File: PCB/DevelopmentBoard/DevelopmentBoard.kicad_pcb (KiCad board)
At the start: 2 copper layers, 128.3 x 64.8 mm, 37 parts, among them IC1 FE1.1S_USB_Controller, J1 Conn_01x04_MountingPin, J2 USB-A, J3 USB-A, J4 CRJ007_RJ45, U1 Pi_CM4, U2 Barometer_Grove, U3 D24V22F5, U4 Micro-USB, U5 VN-100_Breakout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

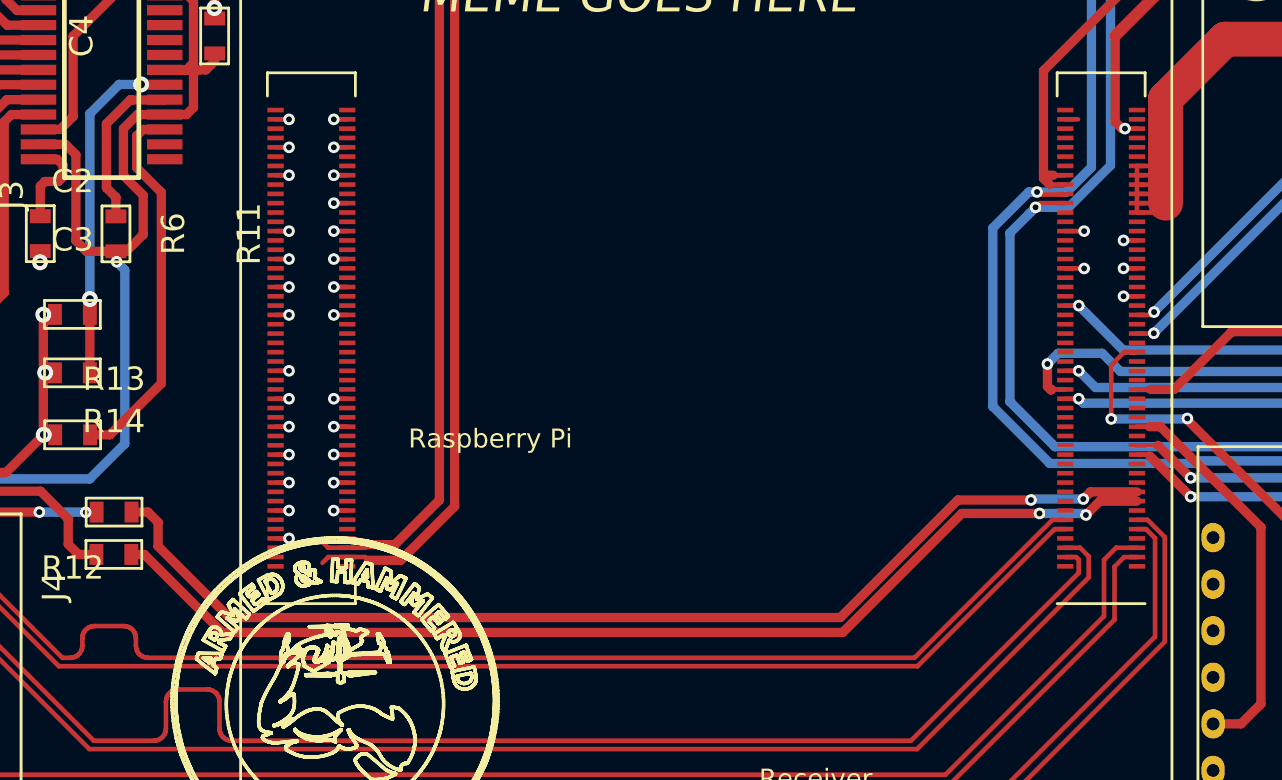
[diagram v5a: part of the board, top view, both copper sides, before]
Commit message: Adjusted USB D0 trace thickness
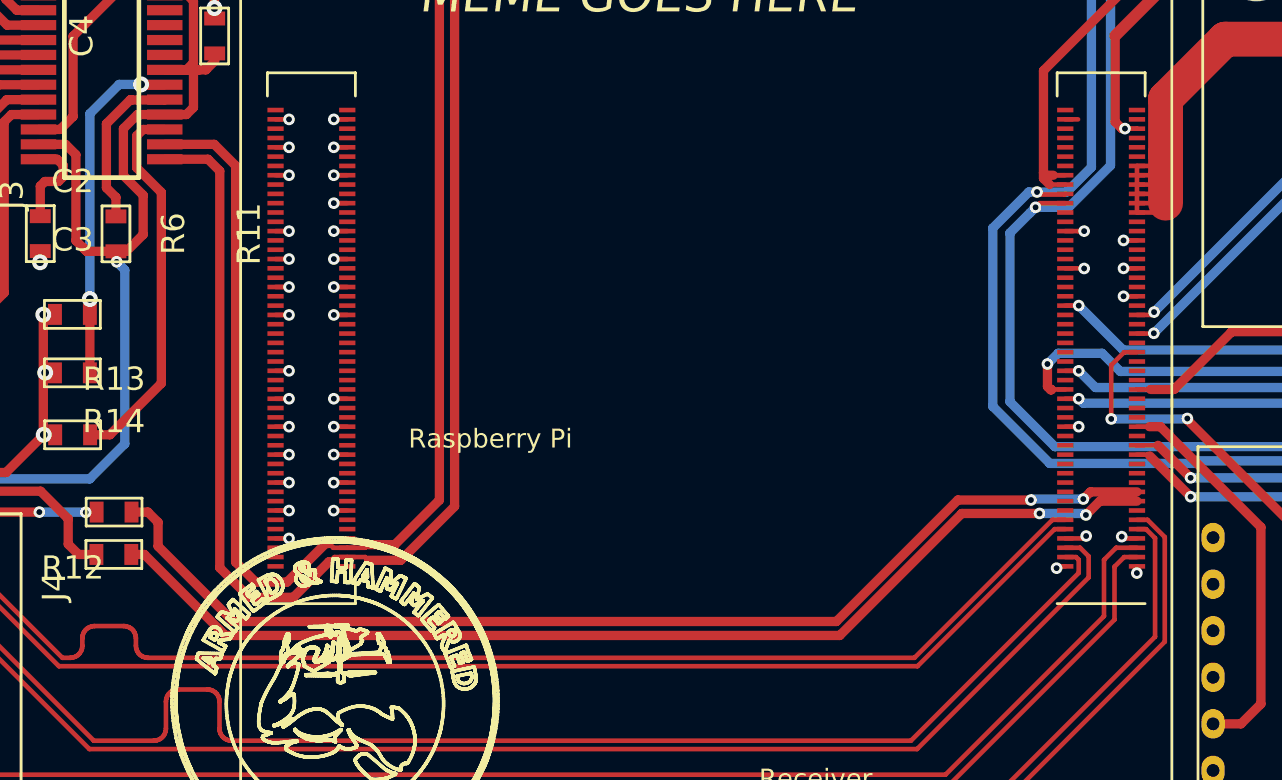
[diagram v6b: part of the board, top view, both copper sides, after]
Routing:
- net /D0+: track 42.8 -> 67.5 mm
- net /D0-: track 45.2 -> 69.9 mm
- net GND: track 27.6 -> 30.5 mm, vias 41 -> 46
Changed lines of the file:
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@@
     (thickness 1.6002)
     (drawings 18801)
-    (tracks 895)
+    (tracks 919)
     (zones 0)
     (modules 37)
@@
   )
   (setup
-    (last_trace_width 0.4)
+    (last_trace_width 0.2)
     (user_trace_width 0.127)
     (user_trace_width 0.2)
@@
   (segment (start 136.926 66.696) (end 137.626 66.696) (width 0.3) (layer Front) (net 2))
   (segment (start 140.216 68.216) (end 140.216 67.036) (width 0.4) (layer Front) (net 2))
+  (via (at 156.46032 103.368) (size 0.5) (drill 0.25) (layers Front Back) (net 2))
+  (segment (start 155.882 103.368) (end 156.46032 103.368) (width 0.2) (layer Front) (net 2))
+  (via (at 155.508665 109.444279) (size 0.5) (drill 0.25) (layers Front Back) (net 2))
+  (segment (start 155.584944 109.368) (end 155.508665 109.444279) (width 0.2) (layer Front) (net 2))
+  (segment (start 155.882 109.368) (end 155.584944 109.368) (width 0.2) (layer Front) (net 2))
+  (via (at 156.779813 108.064004) (size 0.5) (drill 0.25) (layers Front Back) (net 2))
+  (segment (start 156.675817 108.168) (end 156.779813 108.064004) (width 0.2) (layer Front) (net 2))
+  (segment (start 155.882 108.168) (end 156.675817 108.168) (width 0.2) (layer Front) (net 2))
+  (via (at 158.956 109.656) (size 0.5) (drill 0.25) (layers Front Back) (net 2))
+  (segment (start 158.962 109.65) (end 158.956 109.656) (width 0.2) (layer Front) (net 2))
+  (segment (start 158.962 109.368) (end 158.962 109.65) (width 0.2) (layer Front) (net 2))
+  (via (at 158.306 108.091) (size 0.5) (drill 0.25) (layers Front Back) (net 2))
+  (segment (start 158.383 108.168) (end 158.306 108.091) (width 0.2) (layer Front) (net 2))
+  (segment (start 158.962 108.168) (end 158.383 108.168) (width 0.2) (layer Front) (net 2))
   (via (at 112.006 103.716) (size 0.6858) (drill 0.3302) (layers Front Back) (net 3))
   (via (at 111.986 98.556) (size 0.6858) (drill 0.3302) (layers Front Back) (net 3))
@@
   (segment (start 137.606 72.186) (end 139.091 70.701) (width 0.254) (layer Front) (net 163))
   (segment (start 133.276 72.186) (end 137.606 72.186) (width 0.254) (layer Front) (net 163))
-  (segment (start 124.516999 108.968) (end 124.520199 108.9712) (width 0.1524) (layer Front) (net 164))
-  (segment (start 125.042 108.968) (end 124.516999 108.968) (width 0.1524) (layer Front) (net 164))
   (segment (start 125.818 108.968) (end 125.956 109.106) (width 0.2) (layer Front) (net 164))
   (segment (start 125.042 108.968) (end 125.818 108.968) (width 0.2) (layer Front) (net 164))
@@
   (segment (start 127.338448 109.106) (end 129.653 106.791448) (width 0.4) (layer Front) (net 164))
   (segment (start 129.653 76.209) (end 130.066 75.796) (width 0.4) (layer Front) (net 164))
-  (segment (start 125.956 109.106) (end 127.338448 109.106) (width 0.4) (layer Front) (net 164))
   (segment (start 130.076 75.036) (end 133.766 71.076) (width 0.4) (layer Back) (net 164))
   (segment (start 130.076 75.786) (end 130.076 75.036) (width 0.4) (layer Back) (net 164))
@@
   (segment (start 134.276 71.076) (end 134.316 71.116) (width 0.4) (layer Front) (net 164))
   (segment (start 133.766 71.076) (end 134.276 71.076) (width 0.4) (layer Front) (net 164))
-  (segment (start 124.224 108.968) (end 123.976 109.216) (width 0.2) (layer Front) (net 164))
-  (segment (start 125.042 108.968) (end 124.224 108.968) (width 0.2) (layer Front) (net 164))
-  (segment (start 124.516999 108.568) (end 124.520199 108.5648) (width 0.1524) (layer Front) (net 165))
-  (segment (start 125.042 108.568) (end 124.516999 108.568) (width 0.1524) (layer Front) (net 165))
+  (segment (start 125.042 108.968) (end 124.492 108.968) (width 0.2) (layer Front) (net 164))
+  (segment (start 124.492 108.968) (end 124.286 109.174) (width 0.2) (layer Front) (net 164))
+  (segment (start 119.061 91.881) (end 117.203 91.881) (width 0.4) (layer Front) (net 164))
+  (segment (start 124.286 109.174) (end 124.250448 109.174) (width 0.4) (layer Front) (net 164))
+  (segment (start 124.250448 109.174) (end 122.727681 110.696767) (width 0.4) (layer Front) (net 164))
+  (segment (start 122.727681 110.696767) (end 120.834319 110.696767) (width 0.4) (layer Front) (net 164))
+  (segment (start 120.834319 110.696767) (end 119.566 109.428448) (width 0.4) (layer Front) (net 164))
+  (segment (start 119.566 109.428448) (end 119.566 92.386) (width 0.4) (layer Front) (net 164))
+  (segment (start 119.566 92.386) (end 119.061 91.881) (width 0.4) (layer Front) (net 164))
+  (segment (start 125.956 109.106) (end 127.338448 109.106) (width 0.4) (layer Front) (net 164))
   (segment (start 125.824 108.568) (end 125.956 108.436) (width 0.2) (layer Front) (net 165))
   (segment (start 125.042 108.568) (end 125.824 108.568) (width 0.2) (layer Front) (net 165))
@@
   (segment (start 128.999 106.520552) (end 128.999 76.219) (width 0.4) (layer Front) (net 165))
   (segment (start 127.083552 108.436) (end 128.999 106.520552) (width 0.4) (layer Front) (net 165))
-  (segment (start 125.956 108.436) (end 127.083552 108.436) (width 0.4) (layer Front) (net 165))
   (segment (start 131.223012 72.113012) (end 128.556 74.780024) (width 0.4) (layer Back) (net 165))
   (segment (start 128.556 74.780024) (end 128.556 75.776) (width 0.4) (layer Back) (net 165))
-  (segment (start 124.218 108.568) (end 125.042 108.568) (width 0.2) (layer Front) (net 165))
-  (segment (start 123.956 108.306) (end 124.218 108.568) (width 0.2) (layer Front) (net 165))
+  (segment (start 125.042 108.568) (end 124.438 108.568) (width 0.2) (layer Front) (net 165))
+  (segment (start 124.438 108.568) (end 124.256 108.386) (width 0.2) (layer Front) (net 165))
+  (segment (start 124.256 108.386) (end 124.113552 108.386) (width 0.4) (layer Front) (net 165))
+  (segment (start 124.113552 108.386) (end 122.456785 110.042767) (width 0.4) (layer Front) (net 165))
+  (segment (start 122.456785 110.042767) (end 121.105215 110.042767) (width 0.4) (layer Front) (net 165))
+  (segment (start 121.105215 110.042767) (end 120.246 109.183552) (width 0.4) (layer Front) (net 165))
+  (segment (start 120.246 109.183552) (end 120.246 92.156) (width 0.4) (layer Front) (net 165))
+  (segment (start 120.246 92.156) (end 119.331 91.241) (width 0.4) (layer Front) (net 165))
+  (segment (start 119.331 91.241) (end 117.203 91.241) (width 0.4) (layer Front) (net 165))
+  (segment (start 125.956 108.436) (end 127.083552 108.436) (width 0.4) (layer Front) (net 165))
   (segment (start 111.856 93.036) (end 111.856 94.326) (width 0.4) (layer Front) (net 167))
   (segment (start 112.056 92.836) (end 111.856 93.036) (width 0.4) (layer Front) (net 167))
@@
   (via (at 156.656 106.476) (size 0.5) (drill 0.25) (layers Front Back) (net 191))
   (segment (start 158.962 106.168) (end 156.964 106.168) (width 0.4) (layer Front) (net 191))
-  (segment (start 146.220694 111.566) (end 151.267704 106.51899) (width 0.4) (layer Front) (net 191))
   (segment (start 154.449385 106.476) (end 154.406395 106.51899) (width 0.4) (layer Back) (net 191))
-  (segment (start 116.916 108.506) (end 119.976 111.566) (width 0.4) (layer Front) (net 191))
-  (segment (start 116.916 107.476) (end 116.916 108.506) (width 0.4) (layer Front) (net 191))
   (segment (start 156.656 106.476) (end 154.449385 106.476) (width 0.4) (layer Back) (net 191))
-  (segment (start 116.476 107.036) (end 116.916 107.476) (width 0.4) (layer Front) (net 191))
   (via (at 154.406395 106.51899) (size 0.5) (drill 0.25) (layers Front Back) (net 191))
-  (segment (start 119.976 111.566) (end 146.220694 111.566) (width 0.4) (layer Front) (net 191))
-  (segment (start 115.776 107.036) (end 116.476 107.036) (width 0.4) (layer Front) (net 191))
   (segment (start 151.267704 106.51899) (end 154.406395 106.51899) (width 0.4) (layer Front) (net 191))
+  (segment (start 146.050694 111.736) (end 151.267704 106.51899) (width 0.4) (layer Front) (net 191))
+  (segment (start 120.146 111.736) (end 146.050694 111.736) (width 0.4) (layer Front) (net 191))
+  (segment (start 116.916 108.506) (end 120.146 111.736) (width 0.4) (layer Front) (net 191))
+  (segment (start 116.476 107.036) (end 116.916 107.476) (width 0.4) (layer Front) (net 191))
+  (segment (start 116.916 107.476) (end 116.916 108.506) (width 0.4) (layer Front) (net 191))
+  (segment (start 115.776 107.036) (end 116.476 107.036) (width 0.4) (layer Front) (net 191))
   (via (at 154.776 107.096) (size 0.5) (drill 0.25) (layers Front Back) (net 192))
   (segment (start 156.704015 107.096) (end 156.769212 107.161197) (width 0.4) (layer Back) (net 192))
@@
   (via (at 156.769212 107.161197) (size 0.5) (drill 0.25) (layers Front Back) (net 192))
   (segment (start 151.436 107.096) (end 154.776 107.096) (width 0.4) (layer Front) (net 192))
-  (segment (start 146.326 112.206) (end 151.436 107.096) (width 0.4) (layer Front) (net 192))
-  (segment (start 119.676 112.206) (end 146.326 112.206) (width 0.4) (layer Front) (net 192))
+  (segment (start 146.196 112.336) (end 151.436 107.096) (width 0.4) (layer Front) (net 192))
+  (segment (start 119.806 112.336) (end 146.196 112.336) (width 0.4) (layer Front) (net 192))
+  (segment (start 116.326 108.856) (end 119.806 112.336) (width 0.4) (layer Front) (net 192))
   (segment (start 115.766 108.856) (end 116.326 108.856) (width 0.4) (layer Front) (net 192))
-  (segment (start 116.326 108.856) (end 119.676 112.206) (width 0.4) (layer Front) (net 192))
 )
